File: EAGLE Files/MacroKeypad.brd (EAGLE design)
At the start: 61 x 46.4 mm, 13 parts, among them IC2 ATMEGA32U4-MU, SW1 CHERRY-MX, SW2 CHERRY-MX, SW3 CHERRY-MX, SW4 CHERRY-MX, SW5 CHERRY-MX, SW6 CHERRY-MX

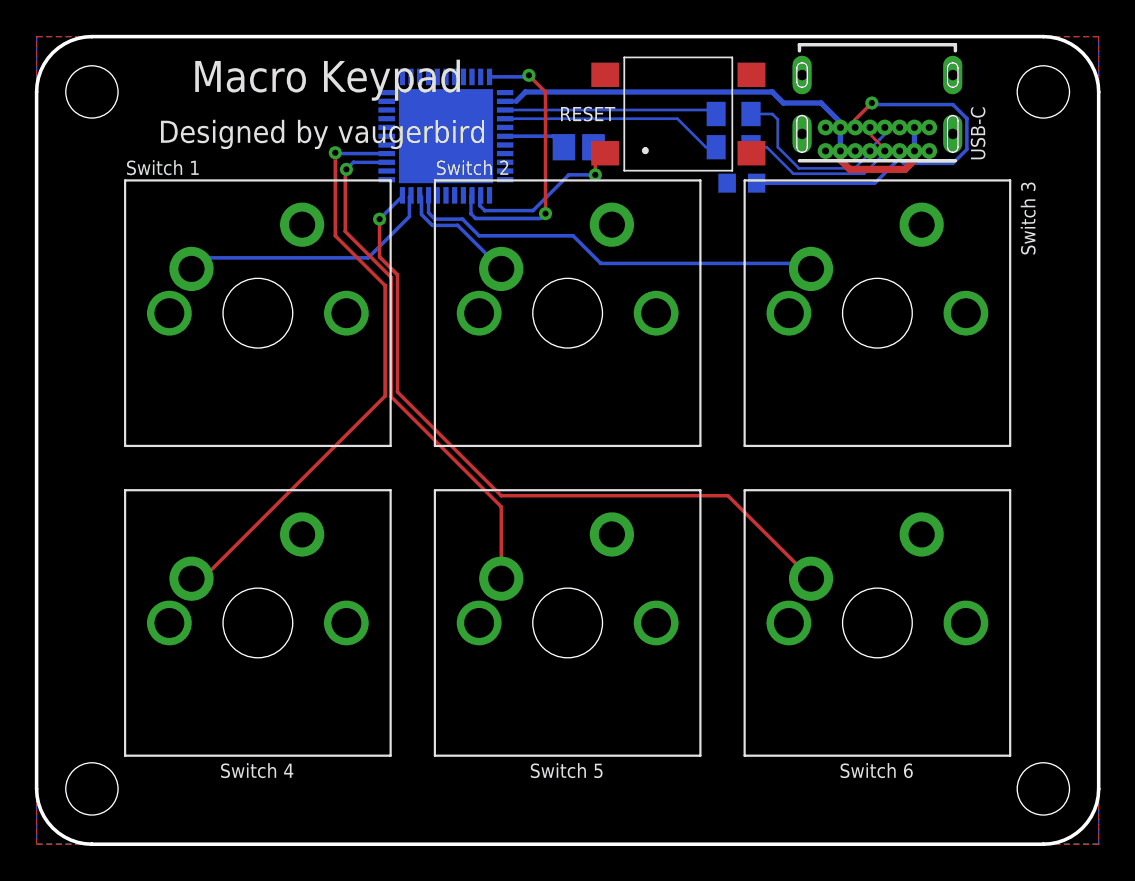
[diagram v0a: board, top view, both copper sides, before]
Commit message: Add programming pads
Also added the BOM as it was missing
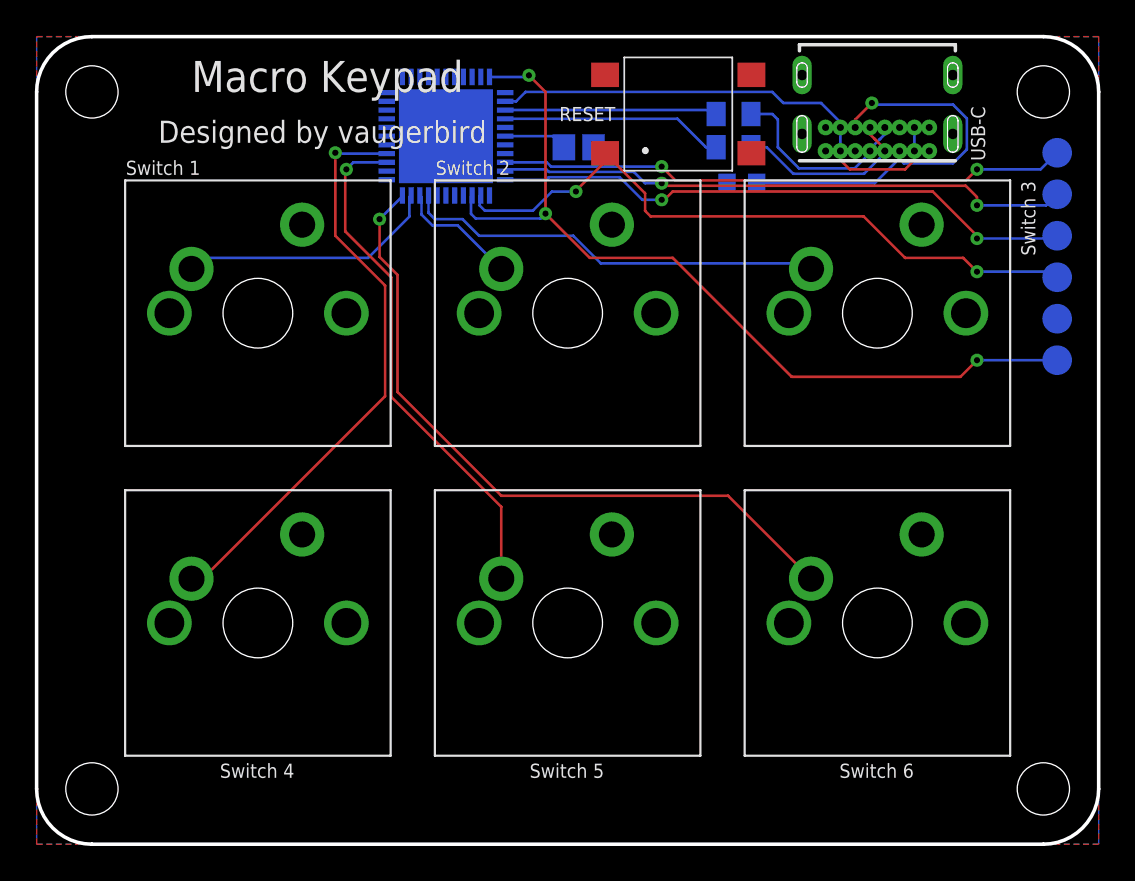
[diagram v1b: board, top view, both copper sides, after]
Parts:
- added 5V, GND, MISO, MOSI, RST, SCLK: TPTP17R, testpad:TP17R
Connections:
- new net MISO: IC2.11, MISO.TP
- new net MOSI: IC2.10, MOSI.TP
- new net SCLK: IC2.9, SCLK.TP
- net GND: now also GND.TP
- net RESET: now also RST.TP
- net VCC: now also 5V.TP
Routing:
- net MISO: track 0.00 -> 33.8 mm, vias 0 -> 2
- net VCC: track 16.2 -> 49.9 mm, vias 2 -> 3
- net MOSI: track 0.00 -> 33.1 mm, vias 0 -> 2
- net SCLK: track 0.00 -> 32.9 mm, vias 0 -> 2
- net RESET: track 9.69 -> 39.1 mm, vias 1 -> 2

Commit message: Fix switch 6 and add switch pinout
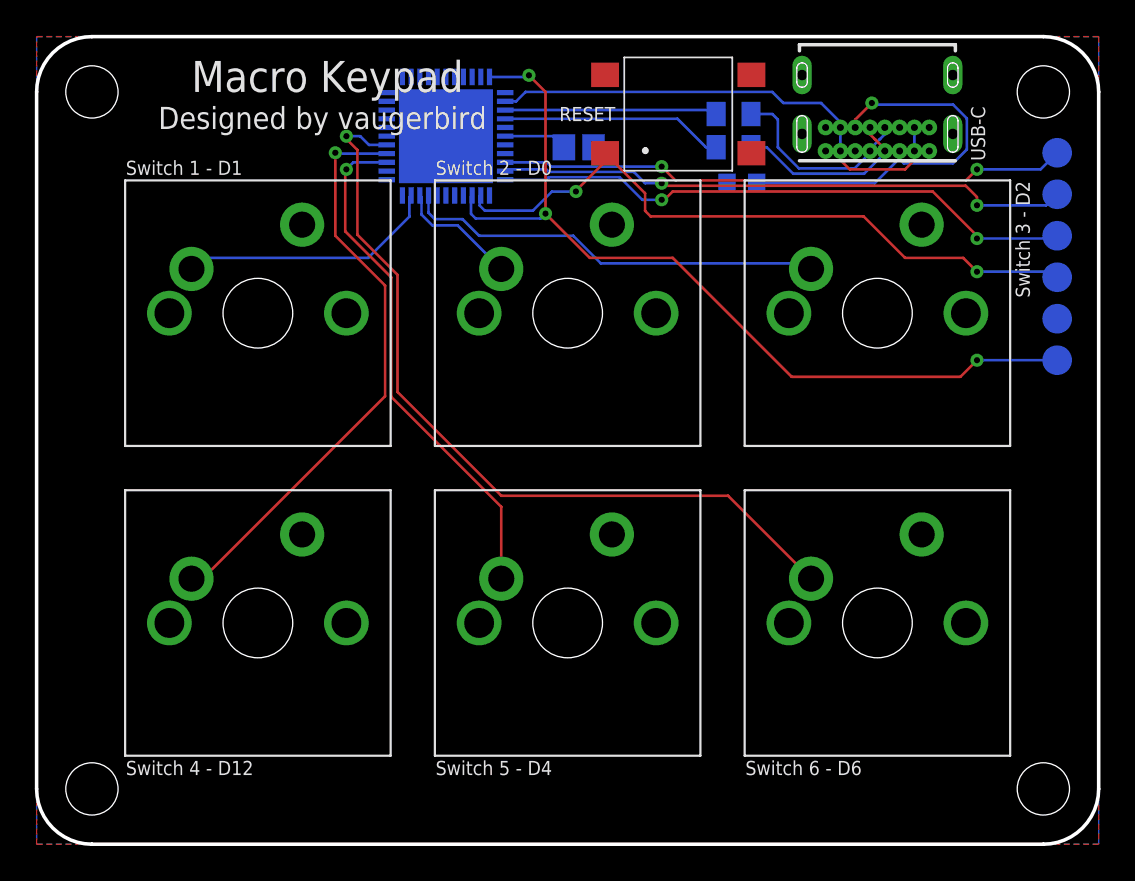
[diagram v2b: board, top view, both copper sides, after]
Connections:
- net SW6: now also IC2.27; no longer IC2.22
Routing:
- net SW6: track 40.4 -> 46.6 mm
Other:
- board text added: "Switch 1 - D1"
- board text added: "Switch 2 - D0"
- board text added: "Switch 3 - D2"
- board text added: "Switch 4 - D12"
- board text added: "Switch 5 - D4"
- board text added: "Switch 6 - D6"
- board text removed: "Switch 1"
- board text removed: "Switch 2"
- board text removed: "Switch 3"
- board text removed: "Switch 4"
- board text removed: "Switch 5"
- board text removed: "Switch 6"
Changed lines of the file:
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@@
 <board>
 <plain>
-<text x="39.411271875" y="67.6275" size="0.8128" layer="25" font="vector">Switch 1</text>
-<text x="57.191271875" y="67.6275" size="0.8128" layer="25" font="vector">Switch 2</text>
-<text x="90.805" y="67.268728125" size="0.8128" layer="25" font="vector" rot="R270">Switch 3</text>
-<text x="44.808771875" y="33.02" size="0.8128" layer="25" font="vector">Switch 4</text>
-<text x="62.588771875" y="33.02" size="0.8128" layer="25" font="vector">Switch 5</text>
-<text x="80.368771875" y="33.02" size="0.8128" layer="25" font="vector">Switch 6</text>
+<text x="39.411271875" y="67.6275" size="0.8128" layer="25" font="vector">Switch 1 - D1</text>
+<text x="57.191271875" y="67.6275" size="0.8128" layer="25" font="vector">Switch 2 - D0</text>
+<text x="90.4875" y="67.268728125" size="0.8128" layer="25" font="vector" rot="R270">Switch 3 - D2</text>
+<text x="39.411271875" y="33.17875" size="0.8128" layer="25" font="vector">Switch 4 - D12</text>
+<text x="57.191271875" y="33.17875" size="0.8128" layer="25" font="vector">Switch 5 - D4</text>
+<text x="74.971271875" y="33.17875" size="0.8128" layer="25" font="vector">Switch 6 - D6</text>
 <wire x1="37.465" y1="29.21" x2="92.075" y2="29.21" width="0.2032" layer="20"/>
 <wire x1="92.075" y1="29.21" x2="95.25" y2="32.385" width="0.2032" layer="20" curve="90"/>
@@
 <hole x="37.465" y="72.39" drill="2.99999375"/>
 <text x="43.18" y="72.39" size="1.778" layer="25" font="vector">Macro Keypad</text>
-<text x="41.275" y="69.469" size="1.27" layer="25" font="vector">Designed by vaugerbird</text>
+<text x="41.275" y="70.26275" size="1.27" layer="25" font="vector">Designed by vaugerbird</text>
 <text x="88.265" y="30.48" size="1.4224" layer="26" font="vector" rot="MR0">Rev 2</text>
 <text x="80.645" y="30.4165" size="1.27" layer="26" font="vector" rot="MR0">https://github.com/vaugerbird/Macro-Keypad</text>
@@
 <signal name="SW6">
 <contactref element="SW6" pad="SW1"/>
-<contactref element="IC2" pad="22"/>
 <wire x1="78.74" y1="44.45" x2="73.9775" y2="49.2125" width="0.1524" layer="1"/>
 <wire x1="55.0037" y1="55.1688" x2="55.0037" y2="61.8896" width="0.1524" layer="1"/>
-<wire x1="53.975" y1="62.9183" x2="53.975" y2="65.0875" width="0.1524" layer="1"/>
-<wire x1="55.0037" y1="61.8896" x2="53.975" y2="62.9183" width="0.1524" layer="1"/>
+<wire x1="52.705" y1="64.1883" x2="52.705" y2="69.05625" width="0.1524" layer="1"/>
+<wire x1="55.0037" y1="61.8896" x2="52.705" y2="64.1883" width="0.1524" layer="1"/>
 <wire x1="73.9775" y1="49.2125" x2="60.96" y2="49.2125" width="0.1524" layer="1"/>
 <wire x1="60.96" y1="49.2125" x2="55.0037" y2="55.1688" width="0.1524" layer="1"/>
-<via x="53.975" y="65.0875" extent="1-16" drill="0.35" shape="octagon"/>
-<wire x1="55.285" y1="66.45" x2="55.285" y2="66.3975" width="0.1524" layer="16"/>
-<wire x1="55.285" y1="66.3975" x2="53.975" y2="65.0875" width="0.1524" layer="16"/>
+<contactref element="IC2" pad="27"/>
+<wire x1="52.705" y1="69.05625" x2="52.07" y2="69.69125" width="0.1524" layer="1"/>
+<wire x1="52.07" y1="69.69125" x2="52.07" y2="69.85" width="0.1524" layer="1"/>
+<via x="52.07" y="69.85" extent="1-16" drill="0.35" shape="octagon"/>
+<wire x1="52.07" y1="69.85" x2="52.86375" y2="69.85" width="0.1524" layer="16"/>
+<wire x1="53.36375" y1="69.35" x2="54.385" y2="69.35" width="0.1524" layer="16"/>
+<wire x1="52.86375" y1="69.85" x2="53.36375" y2="69.35" width="0.1524" layer="16"/>
 </signal>
 <signal name="RESET">
